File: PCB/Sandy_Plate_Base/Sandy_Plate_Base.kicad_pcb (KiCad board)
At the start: 2 copper layers, 302.4 x 93 mm, 1 part

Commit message: 変更：最下行左右端それぞれ2キーの枠をなくす #86
捨て基板への接続箇所を、弱い箇所を避けるように調整
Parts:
- REF**: footprint locallib:60_Outline-Sandy-Plate-Base4 -> locallib:60_Outline-Sandy-Plate-Base5
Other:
- outline, holes or cut-outs redrawn

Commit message: 変更：製造コスト削減のため、あまり補強の意味がない左、右、下の捨て板を削除
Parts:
- REF**: footprint locallib:60_Outline-Sandy-Plate-Base5 -> locallib:60_Outline-Sandy-Plate-Base6
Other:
- board size 302.4 x 93 mm -> 285 x 84.3 mm

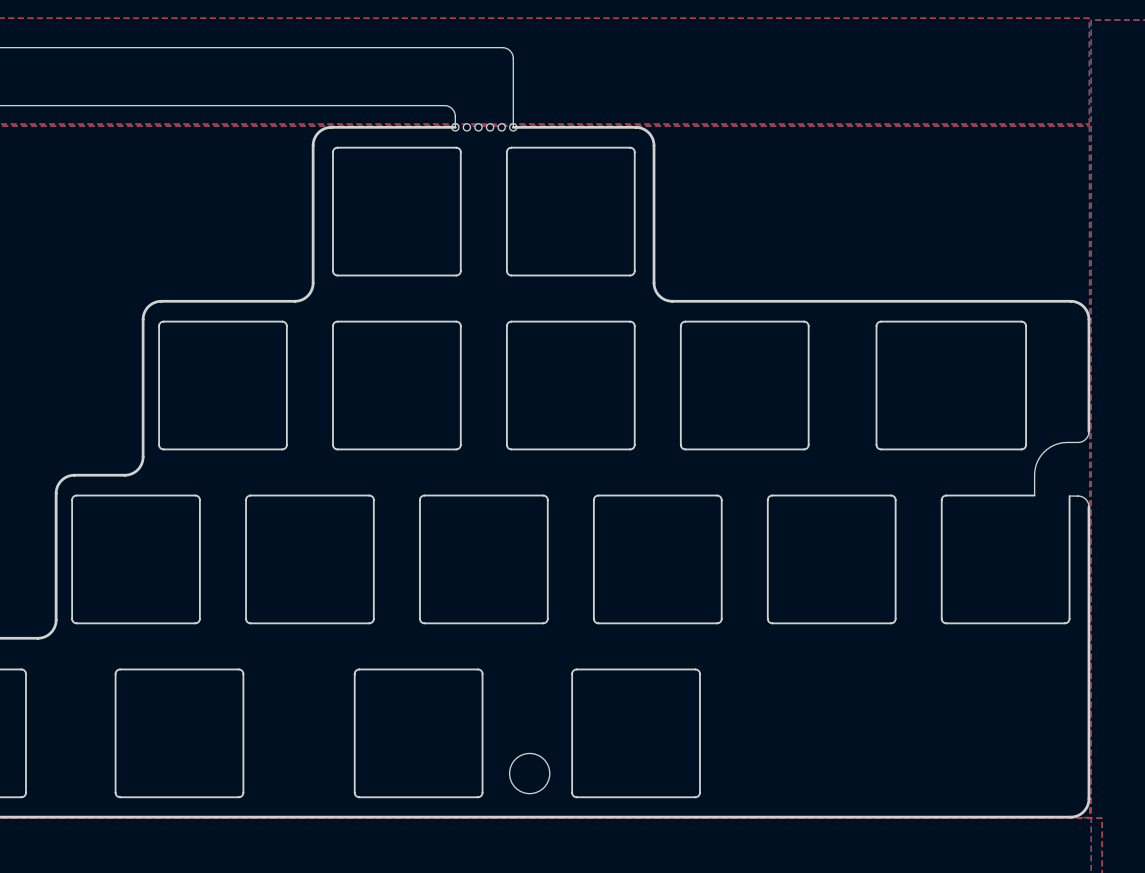
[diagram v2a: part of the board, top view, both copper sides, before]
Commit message: 変更：Base用プレートにロービジのロゴ追加
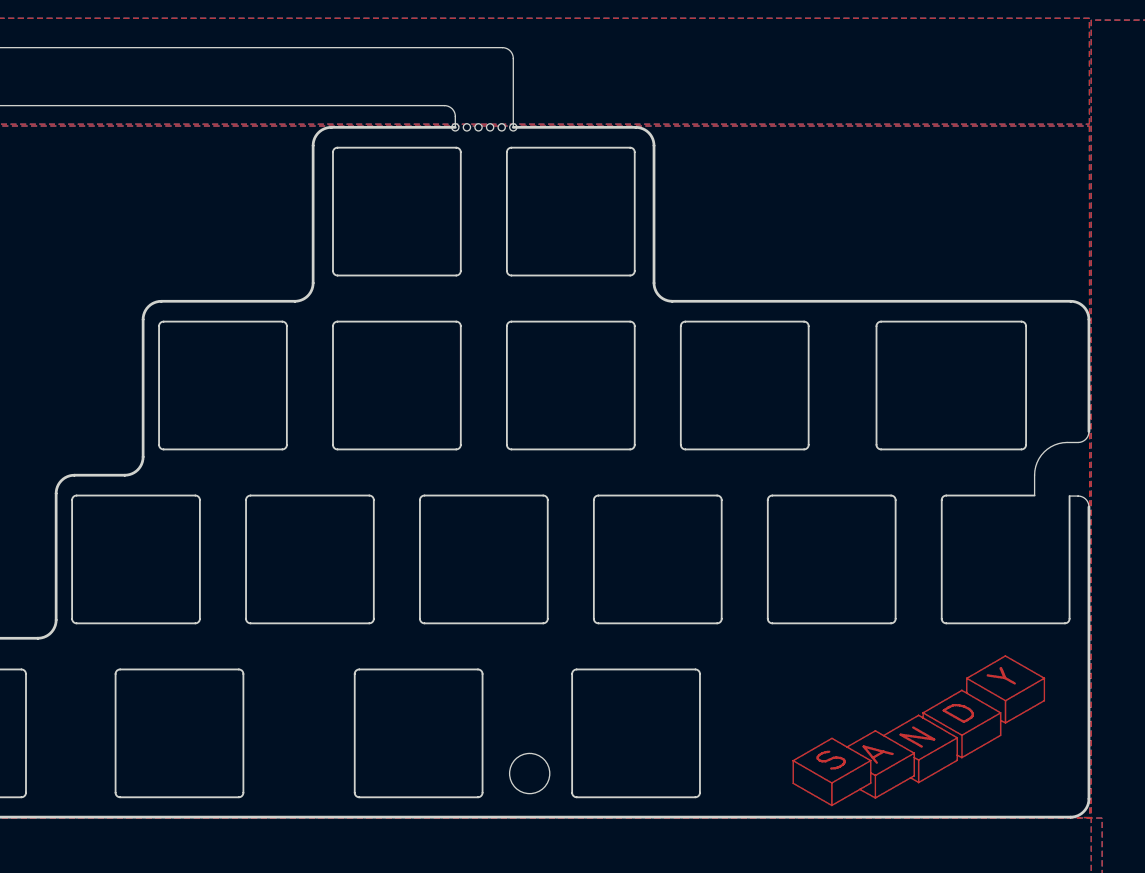
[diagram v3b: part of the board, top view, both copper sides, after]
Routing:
- net (no net): track 0.00 -> 184.8 mm
